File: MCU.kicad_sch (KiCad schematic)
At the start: 0 parts

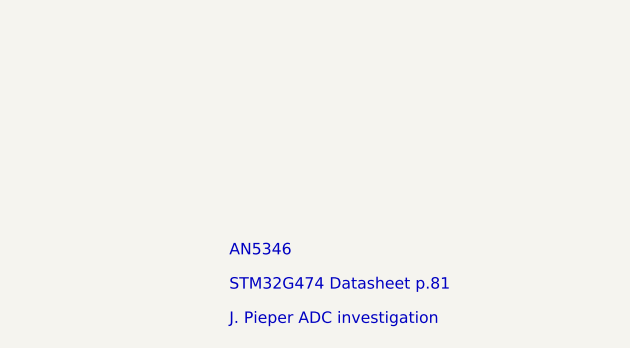
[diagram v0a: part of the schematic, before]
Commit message: [Project][Added] CI/CD environment
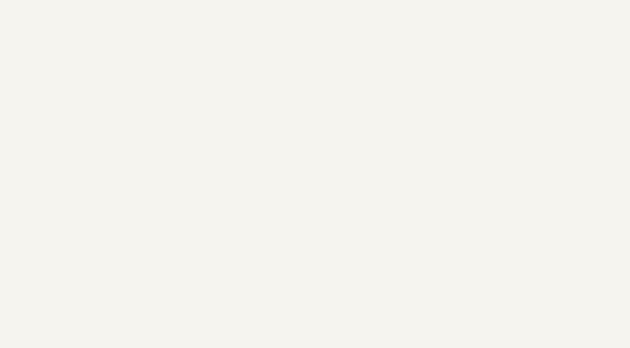
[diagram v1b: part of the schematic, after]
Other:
- note removed: "AN5346"
- note removed: "J. Pieper ADC investigation"
- note removed: "STM32G474 Datasheet p.81"
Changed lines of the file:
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@@
 (kicad_sch
-	(version 20260306)
+	(version 20250114)
 	(generator "eeschema")
-	(generator_version "10.0")
+	(generator_version "9.0")
 	(paper "A4")
 	(title_block
@@
 		(company "${COMPANY}")
 	)
-	(text "J. Pieper ADC investigation"
-		(exclude_from_sim no)
-		(at 142.24 170.18 0)
-		(effects
-			(font
-				(face "Arial")
-				(size 1.27 1.27)
-				(color 0 0 0 1)
-			)
-			(justify left bottom)
-			(href "https://jpieper.com/2023/07/24/stm32g4-adc-performance-part-2/")
-		)
-	)
-	(text "STM32G474 Datasheet p.81"
-		(exclude_from_sim no)
-		(at 142.24 166.37 0)
-		(effects
-			(font
-				(face "Arial")
-				(size 1.27 1.27)
-				(color 0 0 0 1)
-			)
-			(justify left bottom)
-			(href "https://www.st.com/resource/en/datasheet/stm32g474cb.pdf")
-		)
-	)
-	(text "AN5346"
-		(exclude_from_sim no)
-		(at 142.24 162.56 0)
-		(effects
-			(font
-				(face "Arial")
-				(size 1.27 1.27)
-				(color 0 0 0 1)
-			)
-			(justify left bottom)
-			(href "https://www.st.com/resource/en/application_note/an5346-stm32g4-adc-use-tips-and-recommendations-stmicroelectronics.pdf")
-		)
-	)
 	(text_box "[${#}] ${TITLE}"
